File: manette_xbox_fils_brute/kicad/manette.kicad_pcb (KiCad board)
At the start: 2 copper layers, 127 x 101.6 mm, 33 parts, among them J1 THB001P, X1 SW_Push, Y1 SW_Push

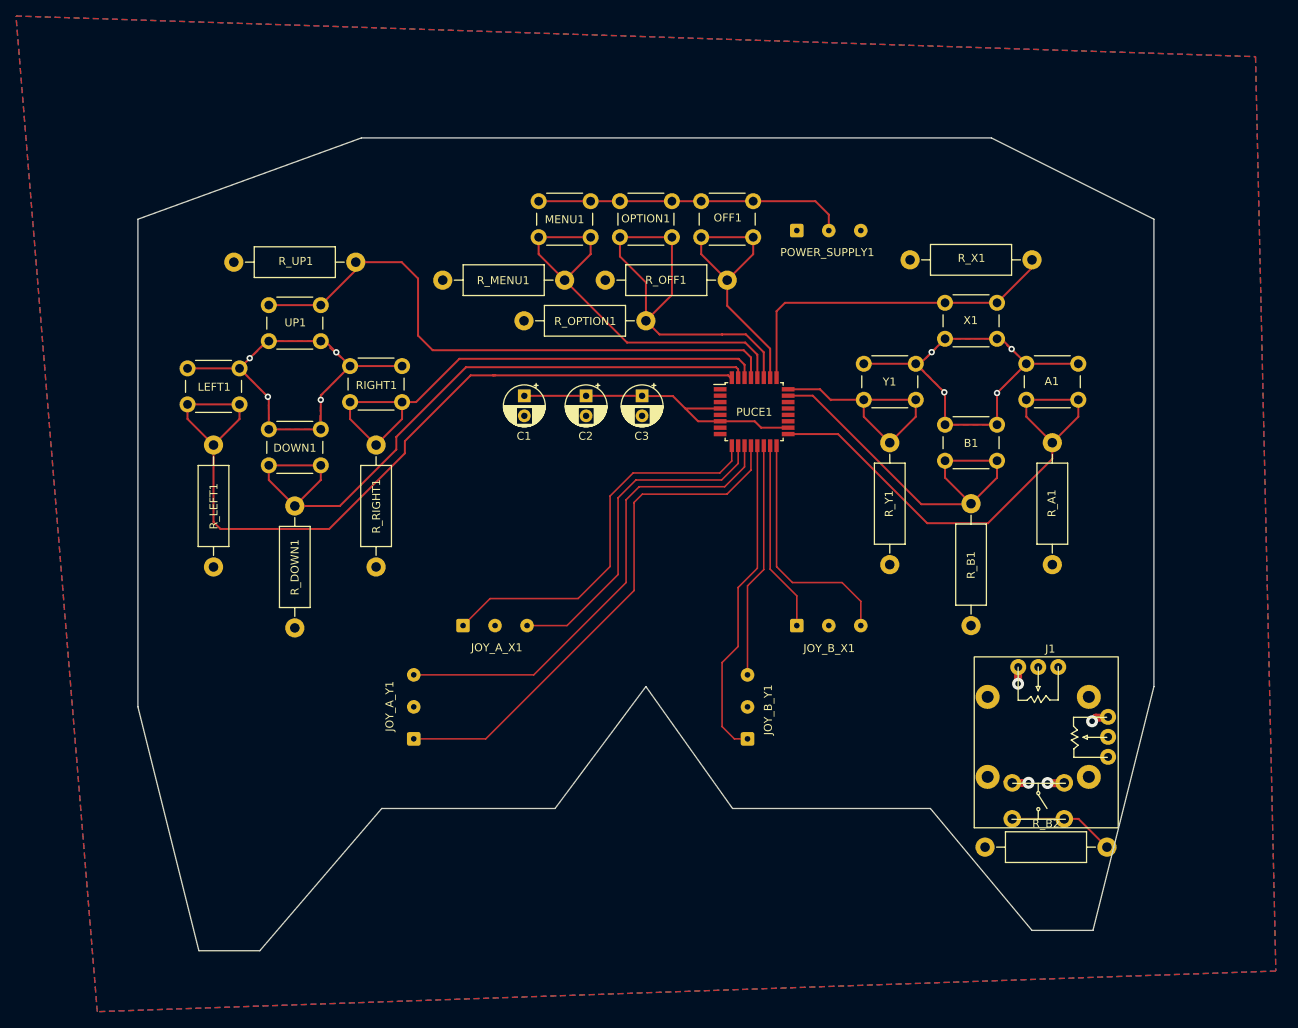
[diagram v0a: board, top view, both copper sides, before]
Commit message: changement en version brut + ajout joystick générique
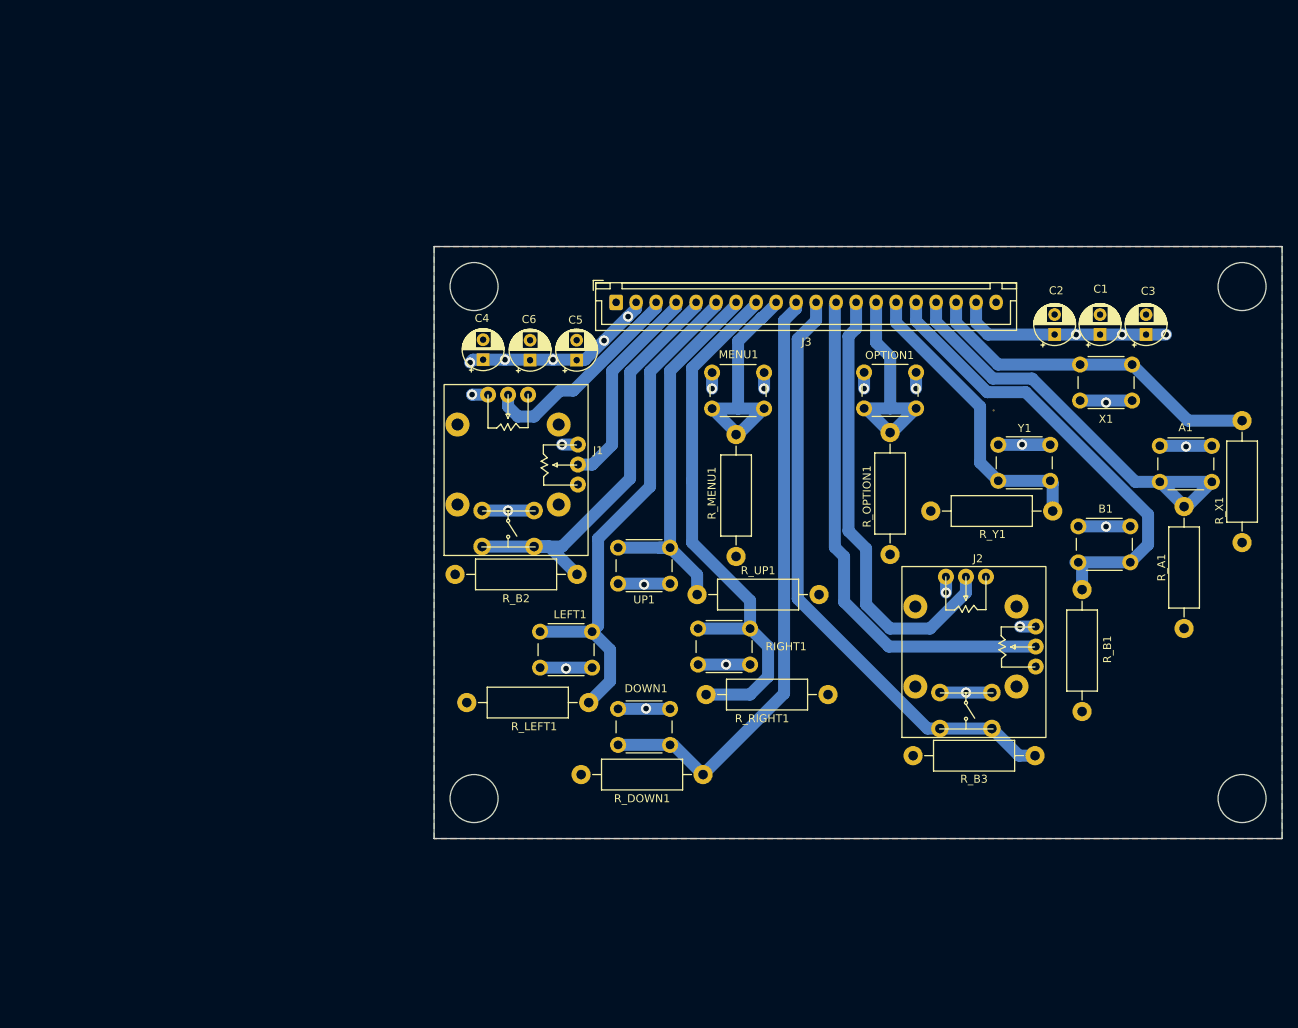
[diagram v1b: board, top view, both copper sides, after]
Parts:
- removed JOY_A_X1, JOY_A_Y1, JOY_B_X1, JOY_B_Y1, POWER_SUPPLY1: Conn_01x03_Female, Connector_Wire:SolderWire-0.15sqmm_1x03_P4mm_D0.5mm_OD1.5mm
- removed OFF1: SW_Push, Button_Switch_THT:SW_PUSH_6mm_H9.5mm
- removed PUCE1: ATmega328P-A, Package_QFP:TQFP-32_7x7mm_P0.8mm
- removed R_OFF1: 100k, Resistor_THT:R_Axial_DIN0411_L9.9mm_D3.6mm_P15.24mm_Horizontal
- added C4: 100p, Capacitor_THT:CP_Radial_D5.0mm_P2.50mm, F.Cu at (137.1, 86.1)
- added C5: 100n, Capacitor_THT:CP_Radial_D5.0mm_P2.50mm, F.Cu at (148.8, 86.2)
- added C6: 10m, Capacitor_THT:CP_Radial_D5.0mm_P2.50mm, F.Cu at (143.0, 86.2)
- added J2: THB001P, LibPerso:Joystick_THB001P, F.Cu at (197.5, 122.0)
- added J3: Conn_01x20, Connector_JST:JST_XH_B20B-XH-A_1x20_P2.50mm_Vertical, F.Cu at (153.8, 79.0)
- added R_B3: 100k, Resistor_THT:R_Axial_DIN0411_L9.9mm_D3.6mm_P15.24mm_Horizontal, F.Cu at (190.9, 135.6)
- moved R_UP1 84.1 mm to (179.1, 115.5), turned to 180 degrees
- moved J1 74.5 mm to (140.2, 99.2)
- moved R_B2 74.5 mm to (133.6, 113.0)
- moved C1 72.4 mm to (214.2, 83.0), turned to 90 degrees
- moved C3 63.5 mm to (220.0, 83.0), turned to 90 degrees
- moved RIGHT1 62.4 mm to (170.5, 124.2), turned to 180 degrees
- moved C2 59.1 mm to (208.6, 83.0), turned to 90 degrees
- moved DOWN1 55.9 mm to (160.5, 134.3)
- moved R_X1 54.5 mm to (232.0, 109.0), turned to 90 degrees
- moved UP1 53.2 mm to (160.5, 114.1)
- moved R_RIGHT1 51.7 mm to (165.0, 128.0), turned to 0 degrees
- moved LEFT1 47.1 mm to (144.2, 120.1), turned to 0 degrees
- moved R_DOWN1 40.2 mm to (149.4, 138.0), turned to 0 degrees
- moved OPTION1 37.3 mm to (184.8, 87.7)
- moved R_LEFT1 35.9 mm to (135.1, 129.0), turned to 0 degrees
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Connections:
- net JOY_C_A renamed JOY_A_A
- DOWN1 pad 1: LEFT -> DOWN
- J1 pad 2: JOY_C_X -> JOY_A_X
- J1 pad 2': JOY_C_Y -> JOY_A_Y
- LEFT1 pad 1: DOWN -> LEFT
- R_DOWN1 pad 2: LEFT -> DOWN
- R_LEFT1 pad 2: DOWN -> LEFT
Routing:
- net JOY_B_A: track 0.00 -> 75.8 mm
- net JOY_A_Y+: track 65.6 -> 0.00 mm
- net JOY_B_Y: track 0.00 -> 64.2 mm
- net 5V: track 196.6 -> 135.8 mm, vias 12 -> 26
- net JOY_A_Y-: track 60.8 -> 0.00 mm
- net JOY_B_X: track 0.00 -> 56.7 mm
- net JOY_A_X-: track 49.2 -> 0.00 mm
- net JOY_A_X+: track 42.6 -> 0.00 mm
- net JOY_A_A: track 13.3 -> 54.3 mm
- net JOY_B_Y+: track 40.8 -> 0.00 mm
- net OFF: track 34.3 -> 0.00 mm
- net JOY_B_X+: track 30.5 -> 0.00 mm
- net JOY_B_Y-: track 29.5 -> 0.00 mm
- net DOWN: track 103.4 -> 76.0 mm
- net JOY_A_X: track 0.00 -> 26.8 mm
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- added copper zone on B.Cu, net GND
- removed copper zone on B.Cu, net 5V
- removed copper zone on F.Cu, net GND
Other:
- board size 127 x 101.6 mm -> 106 x 74 mm

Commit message: redimensionnement de la carte
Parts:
- removed C1, C4: 100p, Capacitor_THT:CP_Radial_D5.0mm_P2.50mm
- removed C2, C5: 100n, Capacitor_THT:CP_Radial_D5.0mm_P2.50mm
- removed C3, C6: 10m, Capacitor_THT:CP_Radial_D5.0mm_P2.50mm
- moved R_B3 51.8 mm to (150.5, 103.2), turned to -90 degrees
- moved X1 42.7 mm to (179.5, 73.4), turned to 0 degrees
- moved R_X1 42.1 mm to (189.9, 106.9)
- moved R_Y1 36.8 mm to (158.5, 92.7)
- moved R_RIGHT1 36.1 mm to (131.5, 114.7)
- moved B1 35.0 mm to (185.8, 98.0)
- moved RIGHT1 35.0 mm to (138.2, 110.8)
- moved R_B1 35.0 mm to (179.7, 116.7)
- moved R_LEFT1 35.0 mm to (102.8, 115.5)
- moved R_UP1 35.0 mm to (146.8, 102.0)
- moved UP1 35.0 mm to (128.2, 100.7)
- moved Y1 35.0 mm to (175.8, 87.8)
- moved A1 35.0 mm to (189.4, 83.5)
- moved DOWN1 35.0 mm to (128.2, 120.8)
- moved J1 35.0 mm to (108.0, 85.8)
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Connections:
- J3 pad 17: A -> X
- J3 pad 18: X -> A
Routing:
- net JOY_B_X: track 56.7 -> 0.00 mm
- net 5V: track 135.8 -> 88.6 mm, vias 26 -> 20
- net OPTION: track 29.5 -> 73.9 mm
- net Y: track 38.4 -> 24.3 mm
- net DOWN: track 76.0 -> 63.2 mm
- net JOY_B_Y: track 64.2 -> 51.7 mm
- net B: track 58.7 -> 47.1 mm
- net JOY_A_A: track 54.3 -> 44.7 mm
- net LEFT: track 65.0 -> 56.5 mm
- net UP: track 49.2 -> 41.6 mm
- net RIGHT: track 69.2 -> 61.7 mm
- net JOY_A_Y: track 26.4 -> 19.0 mm
- net JOY_B_A: track 75.8 -> 81.9 mm
- net A: track 54.3 -> 56.3 mm
- net X: track 43.3 -> 45.0 mm
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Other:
- board size 106 x 74 mm -> 100 x 53 mm
